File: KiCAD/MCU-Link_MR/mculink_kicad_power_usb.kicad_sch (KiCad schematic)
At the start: 39 parts, among them J9 USB4110-GF-A_REVB, U1 LPC55S69JBD64, U2 XC6227C331PR-G, Y1 16.000MHz

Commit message: completed BOM
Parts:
- C1: value 4.7uF -> 4.7uF 6.3V; mouser# (none) -> 581-06033D475KAT2A
- C10, C26, C7, C8, C9: value 10n -> 10nF 6.3V; mouser# (none) -> 80-C0603C103M5R
- C11, C12: value 8p -> 8pF 6.3V; mouser# (none) -> 810-C1608C0G1H080D
- C13, C17, C2, C20, C23, C24, C3, C4, C5, C6: value 100n -> 100nF 6.3V; mouser# (none) -> 80-C0603C104K9R
- C14, C16, C21: value 47p -> 47pF 6.3V; mouser# (none) -> 80-C0603C470M5HACTU
- C15, C19: value 22u -> 22uF 6.3V; mouser# (none) -> 80-C0805C226K9PACTU
- C18: value 22u -> 22uF 6.3V; mouser# (none) -> 581-KGM15CR50J226MT
- C22, C25: value 10u -> 10uF 6.3V; mouser# (none) -> 581-06036D106MAT2A
- D1: value PRTR5V0U2X -> PRTR5V0U2X-QR; mouser# (none) -> 771-PRTR5V0U2X-QR
- L1, L3, L4: value MI0603J601R-10 -> MPZ1608S331ATD25; mouser# (none) -> 810-MPZ1608S331ATD25
- L2: value 4u7 -> 4.6uH; mouser# (none) -> 70-ILSB0805ER4R7K
- R1: value 10k -> 10k 5% 100mW; mouser# (none) -> 667-ERJ-3GEYJ103V
- R2: value 20k -> 20k 5% 100mW; mouser# (none) -> 652-CR0603JW-203ELF
- R4, R7: value 5k1 -> 5.1k 5% 100mW; mouser# (none) -> 652-CR0603JW-512ELF
- U1: mouser# (none) -> 771-LPC55S69JBD64K
- U2: mouser# (none) -> 865-XC6227C331PR-G
- Y1: value 16.000MHz -> NX3225GB-16M-STD-CRA-2; mouser# (none) -> 344-NX3225GB16MSTRA2

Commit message: updates for v0.3: added RTS/CTS signals for J11
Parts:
- C2: footprint Capacitor_SMD:C_0603_1608Metric -> Capacitor_SMD:C_0402_1005Metric
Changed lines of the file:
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@@
 			)
 		)
-		(property "Footprint" "Capacitor_SMD:C_0603_1608Metric"
+		(property "Footprint" "Capacitor_SMD:C_0402_1005Metric"
 			(at 63.1952 45.72 0)
 			(effects

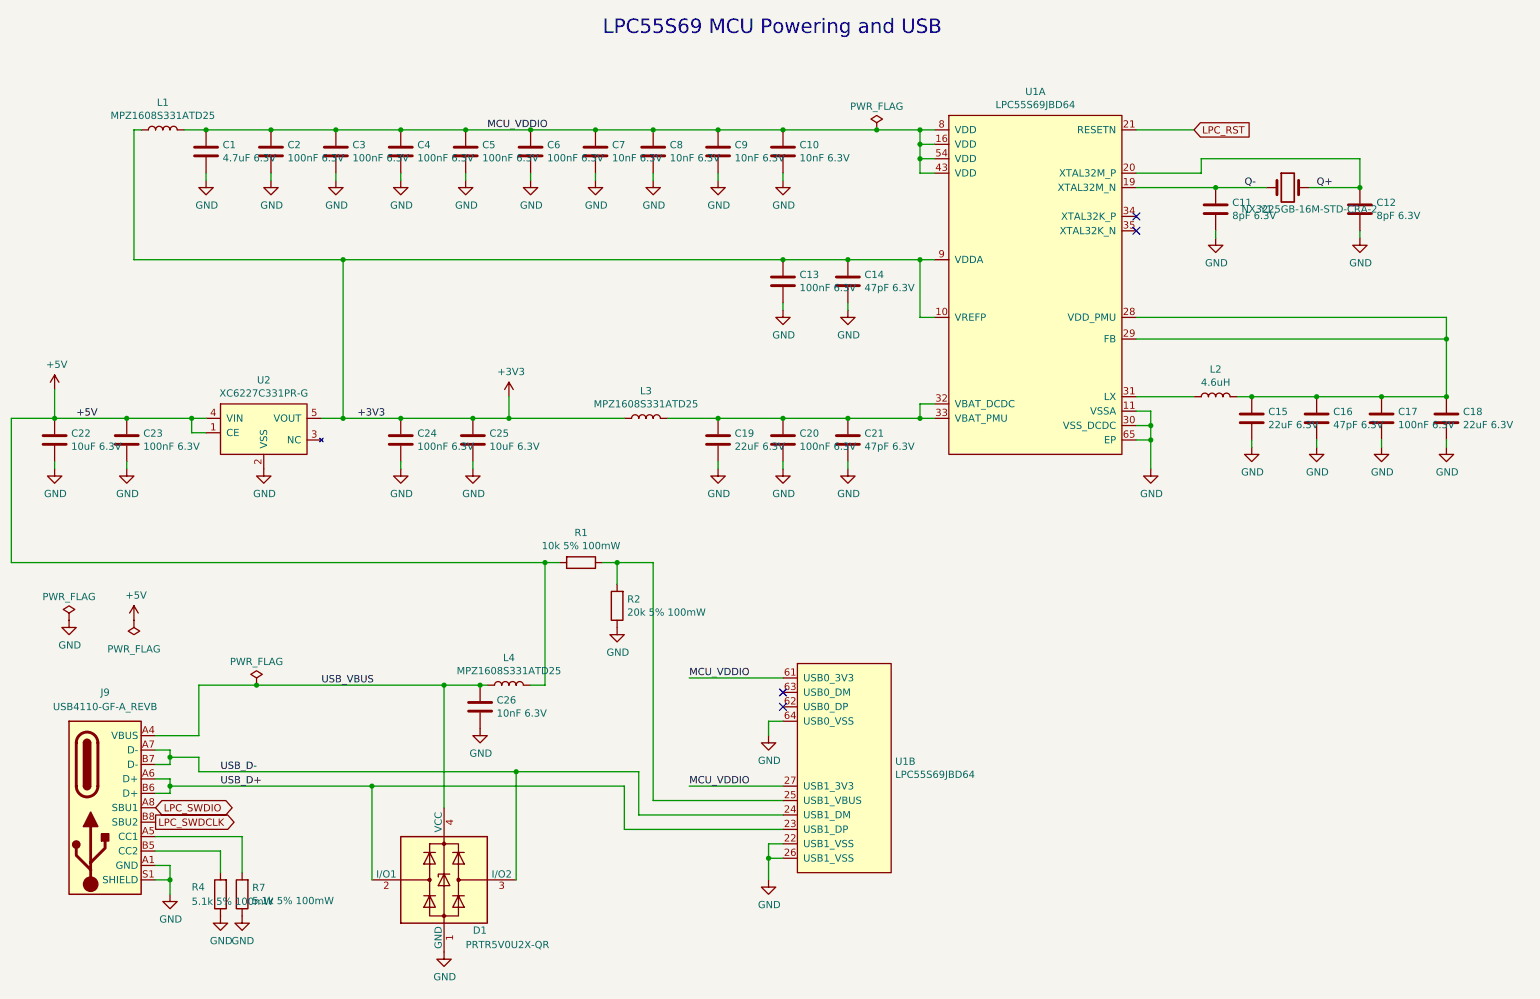
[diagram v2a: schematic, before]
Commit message: simplified footprints
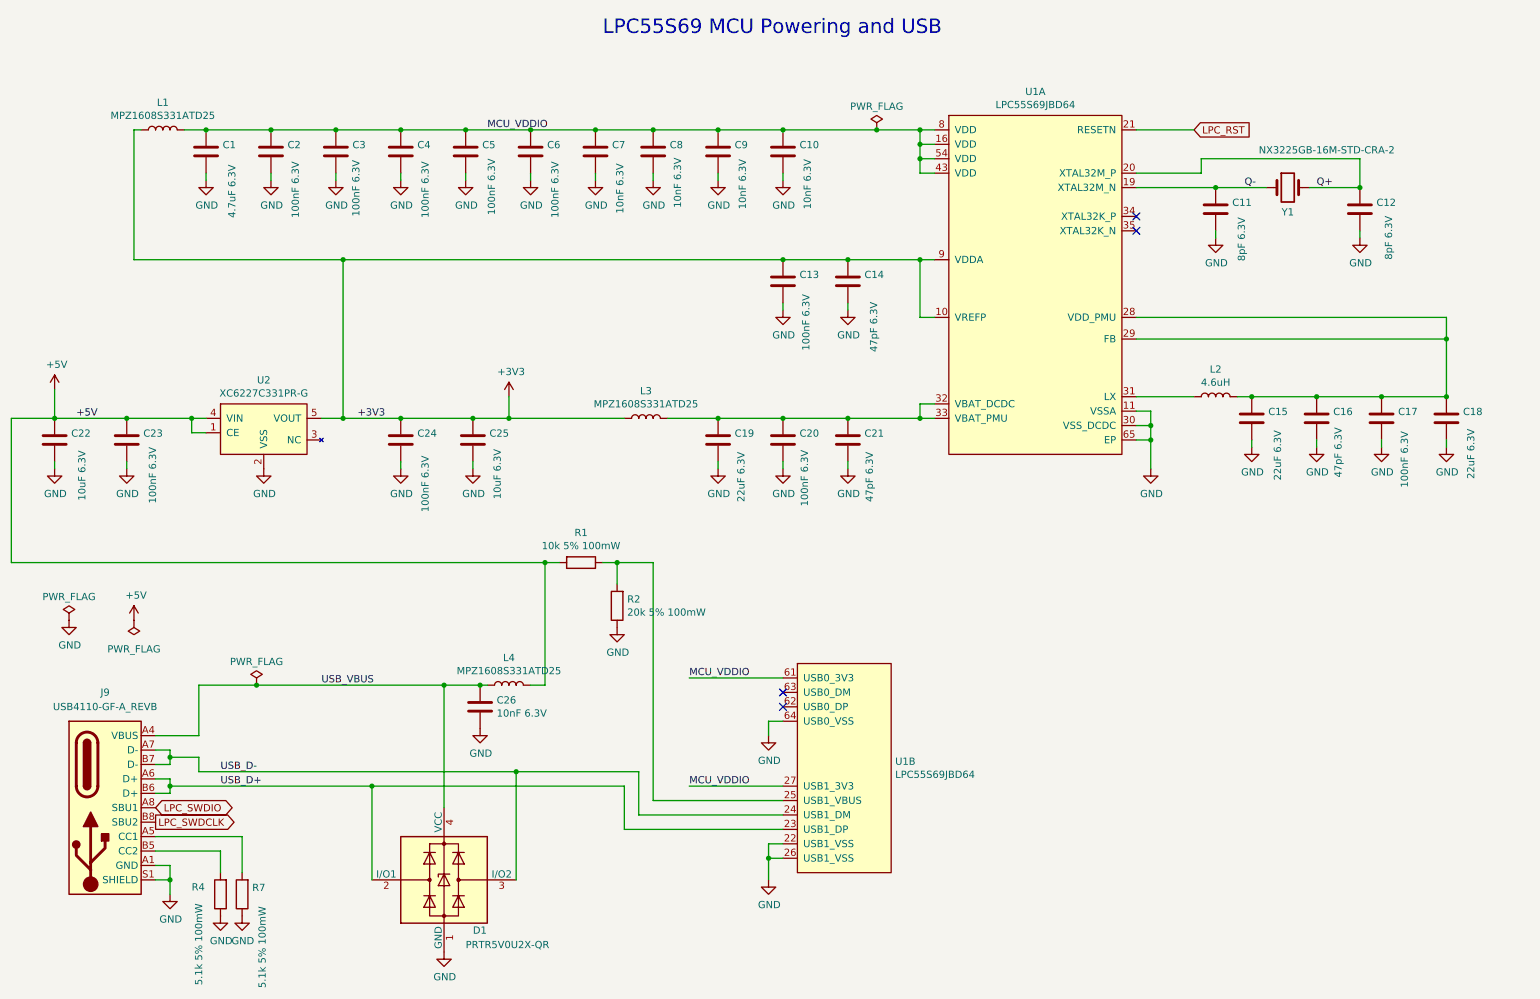
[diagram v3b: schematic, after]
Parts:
- C15, C19: footprint Capacitor_SMD:C_0805_2012Metric -> Capacitor_SMD:C_0603_1608Metric; mouser# 80-C0805C226K9PACTU -> 581-KGM15CR50J226MT
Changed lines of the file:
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@@
 		)
 		(property "Value" "100nF 6.3V"
-			(at 260.731 90.043 0)
+			(at 261.874 101.092 90)
 			(effects
 				(font
@@
 		)
 		(property "Value" "47pF 6.3V"
-			(at 249.301 90.043 0)
+			(at 250.19 99.314 90)
 			(effects
 				(font
@@
 		)
 		(property "Value" "22uF 6.3V"
-			(at 237.871 90.043 0)
+			(at 239.522 99.822 90)
 			(effects
 				(font
@@
 			)
 		)
-		(property "Footprint" "Capacitor_SMD:C_0805_2012Metric"
+		(property "Footprint" "Capacitor_SMD:C_0603_1608Metric"
 			(at 235.9152 92.71 0)
 			(effects
@@
 			)
 		)
-		(property "mouser#" "80-C0805C226K9PACTU"
+		(property "mouser#" "581-KGM15CR50J226MT"
 			(at 234.95 88.9 0)
 			(effects
@@
 		)
 		(property "Value" "22uF 6.3V"
-			(at 272.161 90.043 0)
+			(at 273.558 99.568 90)
 			(effects
 				(font
@@
 		)
 		(property "Value" "8pF 6.3V"
-			(at 231.521 53.213 0)
+			(at 233.172 61.214 90)
 			(effects
 				(font
@@
 		(dnp no)
 		(property "Reference" "Y1"
-			(at 237.49 52.07 0)
+			(at 241.3 52.578 0)
 			(effects
 				(font
@@
 		)
 		(property "Value" "NX3225GB-16M-STD-CRA-2 "
-			(at 245.11 52.07 0)
+			(at 248.158 41.656 0)
 			(effects
 				(font
@@
 		)
 		(property "Value" "8pF 6.3V"
-			(at 256.921 53.213 0)
+			(at 259.08 60.96 90)
 			(effects
 				(font
@@
 		)
 		(property "Value" "100nF 6.3V"
-			(at 39.751 93.853 0)
+			(at 41.402 103.886 90)
 			(effects
 				(font
@@
 		)
 		(property "Value" "10uF 6.3V"
-			(at 27.051 93.853 0)
+			(at 28.956 103.378 90)
 			(effects
 				(font
@@
 		)
 		(property "Value" "100nF 6.3V"
-			(at 88.011 93.853 0)
+			(at 89.408 105.41 90)
 			(effects
 				(font
@@
 		)
 		(property "Value" "10uF 6.3V"
-			(at 100.711 93.853 0)
+			(at 102.108 103.124 90)
 			(effects
 				(font
@@
 		)
 		(property "Value" "4.7uF 6.3V"
-			(at 53.721 43.053 0)
+			(at 55.372 53.594 90)
 			(effects
 				(font
@@
 		)
 		(property "Value" "100nF 6.3V"
-			(at 65.151 43.053 0)
+			(at 66.548 53.594 90)
 			(effects
 				(font
@@
 		)
 		(property "Value" "100nF 6.3V"
-			(at 76.581 43.053 0)
+			(at 77.216 53.34 90)
 			(effects
 				(font
@@
 		)
 		(property "Value" "100nF 6.3V"
-			(at 88.011 43.053 0)
+			(at 89.408 53.594 90)
 			(effects
 				(font
@@
 		)
 		(property "Value" "100nF 6.3V"
-			(at 99.441 43.053 0)
+			(at 101.092 53.086 90)
 			(effects
 				(font
@@
 		)
 		(property "Value" "100nF 6.3V"
-			(at 110.871 43.053 0)
+			(at 112.268 53.594 90)
 			(effects
 				(font
@@
 		)
 		(property "Value" "10nF 6.3V"
-			(at 122.301 43.053 0)
+			(at 123.698 52.832 90)
 			(effects
 				(font
@@
 		)
 		(property "Value" "10nF 6.3V"
-			(at 132.461 43.053 0)
+			(at 133.858 51.816 90)
 			(effects
 				(font
@@
 		)
 		(property "Value" "10nF 6.3V"
-			(at 143.891 43.053 0)
+			(at 145.288 52.07 90)
 			(effects
 				(font
@@
 		)
 		(property "Value" "10nF 6.3V"
-			(at 155.321 43.053 0)
+			(at 156.718 52.07 90)
 			(effects
 				(font
@@
 		)
 		(property "Value" "100nF 6.3V"
-			(at 155.321 65.913 0)
+			(at 156.464 76.962 90)
 			(effects
 				(font
@@
 		)
 		(property "Value" "47pF 6.3V"
-			(at 166.751 65.913 0)
+			(at 168.402 77.216 90)
 			(effects
 				(font
@@
 		)
 		(property "Value" "100nF 6.3V"
-			(at 155.321 93.853 0)
+			(at 156.21 104.394 90)
 			(effects
 				(font
@@
 		)
 		(property "Value" "47pF 6.3V"
-			(at 166.751 93.853 0)
+			(at 167.64 103.632 90)
 			(effects
 				(font
@@
 		)
 		(property "Value" "22uF 6.3V"
-			(at 143.891 93.853 0)
+			(at 145.034 103.632 90)
 			(effects
 				(font
@@
 			)
 		)
-		(property "Footprint" "Capacitor_SMD:C_0805_2012Metric"
+		(property "Footprint" "Capacitor_SMD:C_0603_1608Metric"
 			(at 141.9352 96.52 0)
 			(effects
@@
 			)
 		)
-		(property "mouser#" "80-C0805C226K9PACTU"
+		(property "mouser#" "581-KGM15CR50J226MT"
 			(at 140.97 92.71 0)
 			(effects
@@
 		)
 		(property "Value" "5.1k 5% 100mW"
-			(at 48.26 173.99 0)
+			(at 49.53 188.722 90)
 			(effects
 				(font
@@
 		)
 		(property "Value" "5.1k 5% 100mW"
-			(at 58.928 173.863 0)
+			(at 60.706 189.23 90)
 			(effects
 				(font

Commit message: new v0.4 with pull-down for cts signal (instead pull-up)
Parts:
- L1, L3, L4: value MPZ1608S331ATD25 -> MPZ1608S331ATD25
- Y1: value NX3225GB-16M-STD-CRA-2 -> NX3225GB-16M-STD-CRA-2
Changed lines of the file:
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@@
 			)
 		)
-		(property "Value" "NX3225GB-16M-STD-CRA-2 "
+		(property "Value" "NX3225GB-16M-STD-CRA-2"
 			(at 248.158 41.656 0)
 			(effects
@@
 			)
 		)
-		(property "Value" "MPZ1608S331ATD25 "
+		(property "Value" "MPZ1608S331ATD25"
 			(at 104.14 133.3754 90)
 			(effects
@@
 			)
 		)
-		(property "Value" "MPZ1608S331ATD25 "
+		(property "Value" "MPZ1608S331ATD25"
 			(at 43.18 35.5854 90)
 			(effects
@@
 			)
 		)
-		(property "Value" "MPZ1608S331ATD25 "
+		(property "Value" "MPZ1608S331ATD25"
 			(at 128.27 86.3854 90)
 			(effects

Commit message: Replaced 0603 with 0402 footprints for C and R; removed designators; shifted components to the left
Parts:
- C1, C10, C11, C12, C13, C14, C15, C16, C17, C18, C19, C20, C21, C22, C23, C24, C25, C26, C3, C4, C5, C6, C7, C8, C9: footprint Capacitor_SMD:C_0603_1608Metric -> Capacitor_SMD:C_0402_1005Metric
- R1, R2, R4, R7: footprint Resistor_SMD:R_0603_1608Metric -> Resistor_SMD:R_0402_1005Metric
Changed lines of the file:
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@@
 			)
 		)
-		(property "Footprint" "Capacitor_SMD:C_0603_1608Metric"
+		(property "Footprint" "Capacitor_SMD:C_0402_1005Metric"
 			(at 258.7752 92.71 0)
 			(effects
@@
 			)
 		)
-		(property "Footprint" "Capacitor_SMD:C_0603_1608Metric"
+		(property "Footprint" "Capacitor_SMD:C_0402_1005Metric"
 			(at 247.3452 92.71 0)
 			(effects
@@
 			)
 		)
-		(property "Footprint" "Capacitor_SMD:C_0603_1608Metric"
+		(property "Footprint" "Capacitor_SMD:C_0402_1005Metric"
 			(at 235.9152 92.71 0)
 			(effects
@@
 			)
 		)
-		(property "Footprint" "Capacitor_SMD:C_0603_1608Metric"
+		(property "Footprint" "Capacitor_SMD:C_0402_1005Metric"
 			(at 270.2052 92.71 0)
 			(effects
@@
 			)
 		)
-		(property "Footprint" "Capacitor_SMD:C_0603_1608Metric"
+		(property "Footprint" "Capacitor_SMD:C_0402_1005Metric"
 			(at 229.5652 55.88 0)
 			(effects
@@
 			)
 		)
-		(property "Footprint" "Capacitor_SMD:C_0603_1608Metric"
+		(property "Footprint" "Capacitor_SMD:C_0402_1005Metric"
 			(at 254.9652 55.88 0)
 			(effects
@@
 			)
 		)
-		(property "Footprint" "Capacitor_SMD:C_0603_1608Metric"
+		(property "Footprint" "Capacitor_SMD:C_0402_1005Metric"
 			(at 100.0252 143.51 0)
 			(effects
@@
 			)
 		)
-		(property "Footprint" "Resistor_SMD:R_0603_1608Metric"
+		(property "Footprint" "Resistor_SMD:R_0402_1005Metric"
 			(at 116.84 112.522 90)
 			(effects
@@
 			)
 		)
-		(property "Footprint" "Resistor_SMD:R_0603_1608Metric"
+		(property "Footprint" "Resistor_SMD:R_0402_1005Metric"
 			(at 124.968 121.92 90)
 			(effects
@@
 			)
 		)
-		(property "Footprint" "Capacitor_SMD:C_0603_1608Metric"
+		(property "Footprint" "Capacitor_SMD:C_0402_1005Metric"
 			(at 37.7952 96.52 0)
 			(effects
@@
 			)
 		)
-		(property "Footprint" "Capacitor_SMD:C_0603_1608Metric"
+		(property "Footprint" "Capacitor_SMD:C_0402_1005Metric"
 			(at 25.0952 96.52 0)
 			(effects
@@
 			)
 		)
-		(property "Footprint" "Capacitor_SMD:C_0603_1608Metric"
+		(property "Footprint" "Capacitor_SMD:C_0402_1005Metric"
 			(at 86.0552 96.52 0)
 			(effects
@@
 			)
 		)
-		(property "Footprint" "Capacitor_SMD:C_0603_1608Metric"
+		(property "Footprint" "Capacitor_SMD:C_0402_1005Metric"
 			(at 98.7552 96.52 0)
 			(effects
@@
 			)
 		)
-		(property "Footprint" "Capacitor_SMD:C_0603_1608Metric"
+		(property "Footprint" "Capacitor_SMD:C_0402_1005Metric"
 			(at 51.7652 45.72 0)
 			(effects
@@
 			)
 		)
-		(property "Footprint" "Capacitor_SMD:C_0603_1608Metric"
+		(property "Footprint" "Capacitor_SMD:C_0402_1005Metric"
 			(at 74.6252 45.72 0)
 			(effects
@@
 			)
 		)
-		(property "Footprint" "Capacitor_SMD:C_0603_1608Metric"
+		(property "Footprint" "Capacitor_SMD:C_0402_1005Metric"
 			(at 86.0552 45.72 0)
 			(effects
@@
 			)
 		)
-		(property "Footprint" "Capacitor_SMD:C_0603_1608Metric"
+		(property "Footprint" "Capacitor_SMD:C_0402_1005Metric"
 			(at 97.4852 45.72 0)
 			(effects
@@
 			)
 		)
-		(property "Footprint" "Capacitor_SMD:C_0603_1608Metric"
+		(property "Footprint" "Capacitor_SMD:C_0402_1005Metric"
 			(at 108.9152 45.72 0)
 			(effects
@@
 			)
 		)
-		(property "Footprint" "Capacitor_SMD:C_0603_1608Metric"
+		(property "Footprint" "Capacitor_SMD:C_0402_1005Metric"
 			(at 120.3452 45.72 0)
 			(effects
@@
 			)
 		)
-		(property "Footprint" "Capacitor_SMD:C_0603_1608Metric"
+		(property "Footprint" "Capacitor_SMD:C_0402_1005Metric"
 			(at 130.5052 45.72 0)
 			(effects
@@
 			)
 		)
-		(property "Footprint" "Capacitor_SMD:C_0603_1608Metric"
+		(property "Footprint" "Capacitor_SMD:C_0402_1005Metric"
 			(at 141.9352 45.72 0)
 			(effects
@@
 			)
 		)
-		(property "Footprint" "Capacitor_SMD:C_0603_1608Metric"
+		(property "Footprint" "Capacitor_SMD:C_0402_1005Metric"
 			(at 153.3652 45.72 0)
 			(effects
@@
 			)
 		)
-		(property "Footprint" "Capacitor_SMD:C_0603_1608Metric"
+		(property "Footprint" "Capacitor_SMD:C_0402_1005Metric"
 			(at 153.3652 68.58 0)
 			(effects
@@
 			)
 		)
-		(property "Footprint" "Capacitor_SMD:C_0603_1608Metric"
+		(property "Footprint" "Capacitor_SMD:C_0402_1005Metric"
 			(at 164.7952 68.58 0)
 			(effects
@@
 			)
 		)
-		(property "Footprint" "Capacitor_SMD:C_0603_1608Metric"
+		(property "Footprint" "Capacitor_SMD:C_0402_1005Metric"
 			(at 153.3652 96.52 0)
 			(effects
@@
 			)
 		)
-		(property "Footprint" "Capacitor_SMD:C_0603_1608Metric"
+		(property "Footprint" "Capacitor_SMD:C_0402_1005Metric"
 			(at 164.7952 96.52 0)
 			(effects
@@
 			)
 		)
-		(property "Footprint" "Capacitor_SMD:C_0603_1608Metric"
+		(property "Footprint" "Capacitor_SMD:C_0402_1005Metric"
 			(at 141.9352 96.52 0)
 			(effects
@@
 			)
 		)
-		(property "Footprint" "Resistor_SMD:R_0603_1608Metric"
+		(property "Footprint" "Resistor_SMD:R_0402_1005Metric"
 			(at 55.118 172.72 90)
 			(effects
@@
 			)
 		)
-		(property "Footprint" "Resistor_SMD:R_0603_1608Metric"
+		(property "Footprint" "Resistor_SMD:R_0402_1005Metric"
 			(at 58.928 172.72 90)
 			(effects
